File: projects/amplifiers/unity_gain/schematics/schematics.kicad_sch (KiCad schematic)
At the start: 3 parts, among them J1 15V, U1 LM741

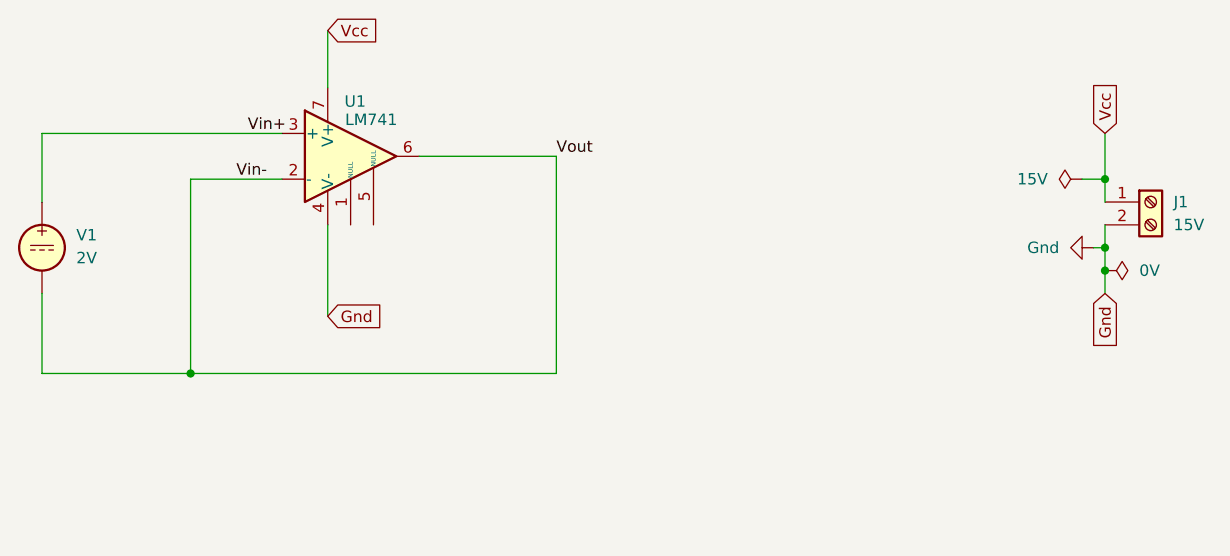
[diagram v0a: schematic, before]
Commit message: feat: Completes the unity gain amplifier design
This completes the design of a unity gain amplifier using an operational
amplifier (op-amp). This updates the components, equipment and
circuit schematic.

Adds practical measurements and analyis of the unity gain amplifier.
Includes measurements inside the LM741 operating range and outside the
operating range to show the limitations of the op-amp in real-world
applications.

Breaking changes: None

Resolves: None
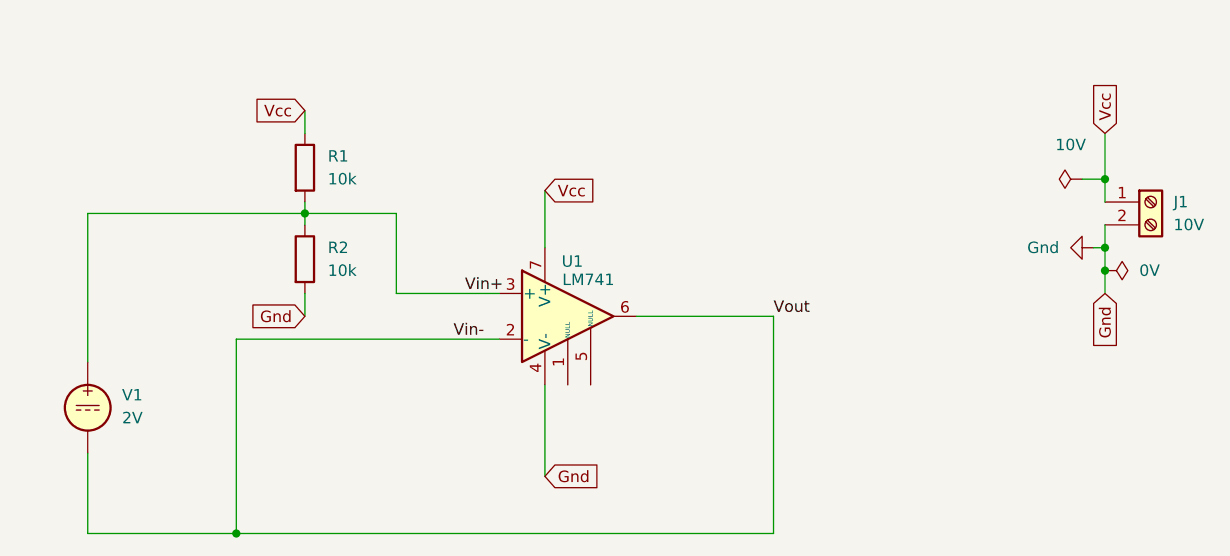
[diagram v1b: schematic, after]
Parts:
- added R1, R2: 10k, symbol Device:R
- J1: value 15V -> 10V
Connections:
- net Gnd: now also R2.2
- net Vcc: now also R1.1
- net Vin+: now also R1.2, R2.1
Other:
- moved on the sheet: U1, V1
